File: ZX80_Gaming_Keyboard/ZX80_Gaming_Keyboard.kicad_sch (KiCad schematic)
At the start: 55 parts, among them J1 KB1, J2 KB2, J3 SPACE_ZERO, SW1 1, SW10 0, SW11 Q, SW12 W, SW13 E, SW14 R, SW15 T, SW16 Y, SW17 U, SW18 I, SW19 O, SW2 2, SW20 P, SW21 A, SW22 S, SW23 D, SW24 F, SW25 G, SW26 H, SW27 J, SW28 K, SW29 L, SW3 3, SW30 NL, SW31 SHIFT, SW32 Z, SW33 X, SW34 C, SW35 V, SW36 B, SW37 N, SW38 M, SW39 DOT, SW4 4, SW40 SPACE, SW41 LEFT, SW42 DOWN, SW43 UP, SW44 RIGHT, SW45 RUBOUT, SW5 5, SW6 6, SW7 7, SW8 8, SW9 9

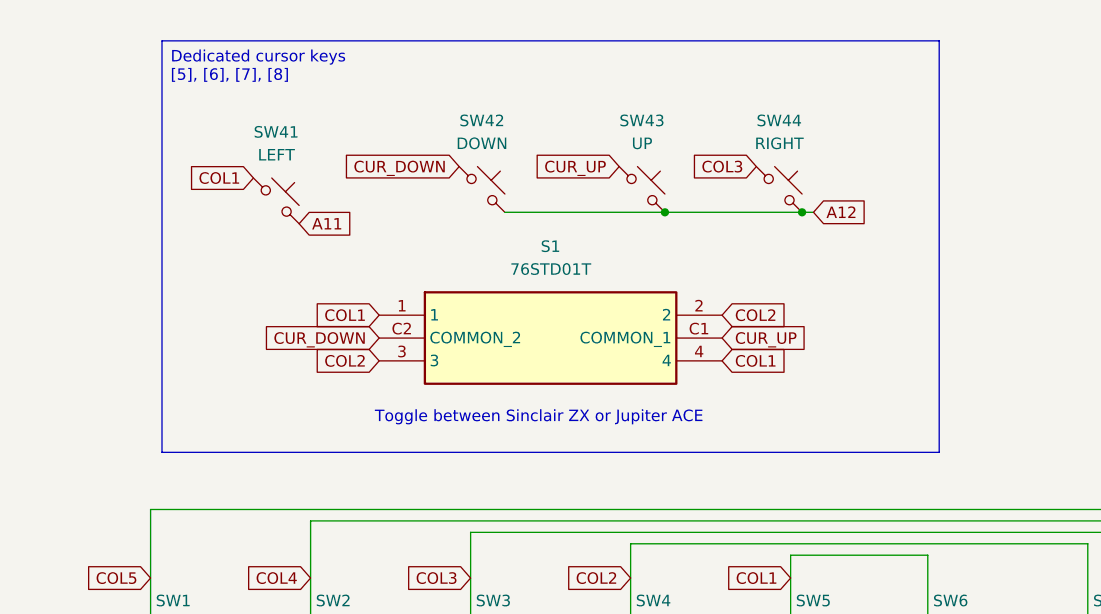
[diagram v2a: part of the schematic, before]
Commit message: Revised ZX/ACE switch
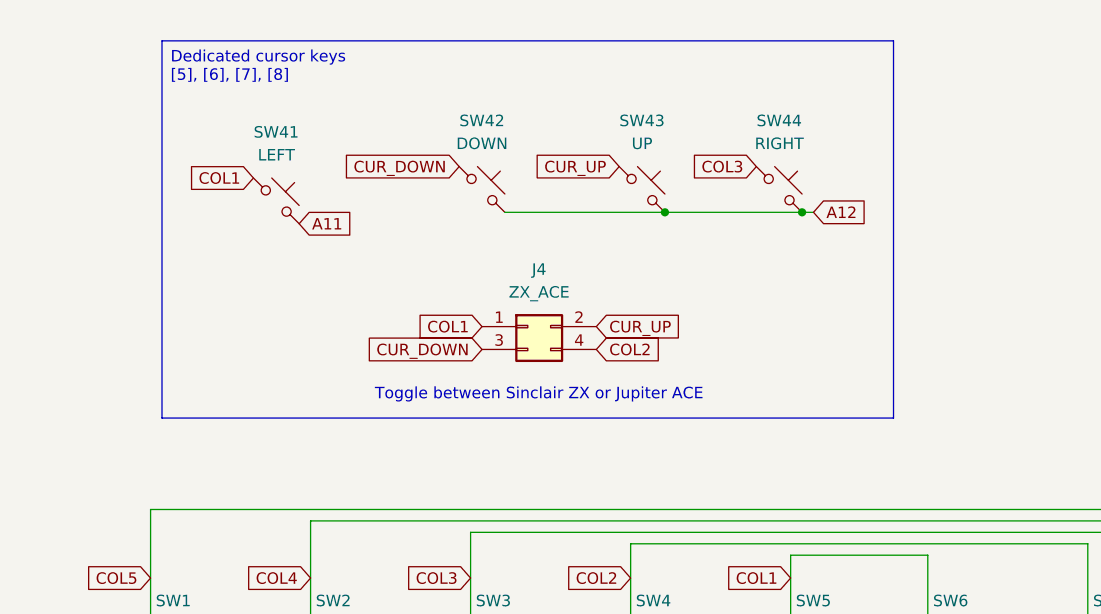
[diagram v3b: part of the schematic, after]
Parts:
- removed S1: 76STD01T, Button_Switch_THT:76STD01T, symbol Switch:76STD01T
- added J4: ZX_ACE, Connector_PinHeader_2.54mm:PinHeader_2x02_P2.54mm_Vertical, symbol Connector_Generic:Conn_02x02_Odd_Even
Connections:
- net COL1: now also J4.1 (Pin_1)
- net COL2: now also J4.4 (Pin_4)
- net CUR_DOWN: now also J4.3 (Pin_3)
- net CUR_UP: now also J4.2 (Pin_2)
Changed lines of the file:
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@@
 	(text "Toggle between Sinclair ZX or Jupiter ACE"
 		(exclude_from_sim no)
-		(at 124.46 62.23 0)
+		(at 124.46 59.69 0)
 		(effects
 			(font
@@
 		(exclude_from_sim no)
 		(at 82.55 20.32 0)
-		(size 86.36 45.72)
+		(size 81.28 41.91)
 		(margins 0.9525 0.9525 0.9525 0.9525)
 		(stroke
@@
 		)
 	)
-	(global_label "COL1"
+	(global_label "A10"
 		(shape input)
-		(at 106.68 50.8 180)
+		(at 123.19 165.1 180)
 		(fields_autoplaced yes)
 		(effects
@@
 		)
 		(property "Intersheetrefs" "${INTERSHEET_REFS}"
-			(at 98.8567 50.8 0)
+			(at 116.6972 165.1 0)
 			(effects
 				(font
@@
 		)
 	)
-	(global_label "A10"
+	(global_label "A11"
 		(shape input)
-		(at 123.19 165.1 180)
+		(at 97.79 40.64 0)
 		(fields_autoplaced yes)
 		(effects
@@
 				(size 1.27 1.27)
 			)
-			(justify right)
+			(justify left)
 		)
 		(property "Intersheetrefs" "${INTERSHEET_REFS}"
-			(at 116.6972 165.1 0)
+			(at 104.2828 40.64 0)
 			(effects
 				(font
 					(size 1.27 1.27)
 				)
-				(justify right)
+				(justify left)
 				(hide yes)
 			)
 		)
 	)
-	(global_label "A11"
+	(global_label "COL1"
 		(shape input)
-		(at 97.79 40.64 0)
+		(at 118.11 52.07 180)
 		(fields_autoplaced yes)
 		(effects
@@
 				(size 1.27 1.27)
 			)
-			(justify left)
+			(justify right)
 		)
 		(property "Intersheetrefs" "${INTERSHEET_REFS}"
-			(at 104.2828 40.64 0)
+			(at 110.2867 52.07 0)
 			(effects
 				(font
 					(size 1.27 1.27)
 				)
-				(justify left)
+				(justify right)
 				(hide yes)
 			)
@@
 		)
 	)
+	(global_label "CUR_DOWN"
+		(shape input)
+		(at 118.11 54.61 180)
+		(fields_autoplaced yes)
+		(effects
+			(font
+				(size 1.27 1.27)
+			)
+			(justify right)
+		)
+		(property "Intersheetrefs" "${INTERSHEET_REFS}"
+			(at 104.9043 54.61 0)
+			(effects
+				(font
+					(size 1.27 1.27)
+				)
+				(justify right)
+				(hide yes)
+			)
+		)
+	)
 	(global_label "A14"
 		(shape input)
@@
 		)
 	)
+	(global_label "COL2"
+		(shape input)
+		(at 130.81 54.61 0)
+		(fields_autoplaced yes)
+		(effects
+			(font
+				(size 1.27 1.27)
+			)
+			(justify left)
+		)
+		(property "Intersheetrefs" "${INTERSHEET_REFS}"
+			(at 138.6333 54.61 0)
+			(effects
+				(font
+					(size 1.27 1.27)
+				)
+				(justify left)
+				(hide yes)
+			)
+		)
+	)
 	(global_label "CUR_UP"
 		(shape input)
-		(at 144.78 53.34 0)
+		(at 130.81 52.07 0)
 		(fields_autoplaced yes)
 		(effects
@@
 		)
 		(property "Intersheetrefs" "${INTERSHEET_REFS}"
-			(at 155.2038 53.34 0)
+			(at 141.2338 52.07 0)
 			(effects
 				(font
@@
 		)
 	)
-	(global_label "COL2"
-		(shape input)
-		(at 144.78 50.8 0)
-		(fields_autoplaced yes)
-		(effects
-			(font
-				(size 1.27 1.27)
-			)
-			(justify left)
-		)
-		(property "Intersheetrefs" "${INTERSHEET_REFS}"
-			(at 152.6033 50.8 0)
-			(effects
-				(font
-					(size 1.27 1.27)
-				)
-				(justify left)
-				(hide yes)
-			)
-		)
-	)
 	(global_label "A9"
 		(shape input)
@@
 		)
 	)
-	(global_label "COL1"
-		(shape input)
-		(at 144.78 55.88 0)
-		(fields_autoplaced yes)
-		(effects
-			(font
-				(size 1.27 1.27)
-			)
-			(justify left)
-		)
-		(property "Intersheetrefs" "${INTERSHEET_REFS}"
-			(at 152.6033 55.88 0)
-			(effects
-				(font
-					(size 1.27 1.27)
-				)
-				(justify left)
-				(hide yes)
-			)
-		)
-	)
 	(global_label "A15"
 		(shape input)
@@
 	(global_label "CUR_DOWN"
 		(shape input)
-		(at 106.68 53.34 180)
-		(fields_autoplaced yes)
-		(effects
-			(font
-				(size 1.27 1.27)
-			)
-			(justify right)
-		)
-		(property "Intersheetrefs" "${INTERSHEET_REFS}"
-			(at 93.4743 53.34 0)
-			(effects
-				(font
-					(size 1.27 1.27)
-				)
-				(justify right)
-				(hide yes)
-			)
-		)
-	)
-	(global_label "CUR_DOWN"
-		(shape input)
 		(at 115.57 34.29 180)
 		(fields_autoplaced yes)
@@
 		)
 	)
-	(global_label "COL2"
-		(shape input)
-		(at 106.68 55.88 180)
-		(fields_autoplaced yes)
-		(effects
-			(font
-				(size 1.27 1.27)
-			)
-			(justify right)
-		)
-		(property "Intersheetrefs" "${INTERSHEET_REFS}"
-			(at 98.8567 55.88 0)
-			(effects
-				(font
-					(size 1.27 1.27)
-				)
-				(justify right)
-				(hide yes)
-			)
-		)
-	)
 	(global_label "COL1"
 		(shape input)
@@
 	)
 	(symbol
+		(lib_id "Connector_Generic:Conn_02x02_Odd_Even")
+		(at 123.19 52.07 0)
+		(unit 1)
+		(exclude_from_sim no)
+		(in_bom yes)
+		(on_board yes)
+		(dnp no)
+		(fields_autoplaced yes)
+		(property "Reference" "J4"
+			(at 124.46 45.72 0)
+			(effects
+				(font
+					(size 1.27 1.27)
+				)
+			)
+		)
+		(property "Value" "ZX_ACE"
+			(at 124.46 48.26 0)
+			(effects
+				(font
+					(size 1.27 1.27)
+				)
+			)
+		)
+		(property "Footprint" "Connector_PinHeader_2.54mm:PinHeader_2x02_P2.54mm_Vertical"
+			(at 123.19 52.07 0)
+			(effects
+				(font
+					(size 1.27 1.27)
+				)
+				(hide yes)
+			)
+		)
+		(property "Datasheet" "~"
+			(at 123.19 52.07 0)
+			(effects
+				(font
+					(size 1.27 1.27)
+				)
+				(hide yes)
+			)
+		)
+		(property "Description" "Generic connector, double row, 02x02, odd/even pin numbering scheme (row 1 odd numbers, row 2 even numbers), script generated (kicad-library-utils/schlib/autogen/connector/)"
+			(at 123.19 52.07 0)
+			(effects
+				(font
+					(size 1.27 1.27)
+				)
+				(hide yes)
+			)
+		)
+		(pin "1"
+		)
+		(pin "3"
+		)
+		(pin "4"
+		)
+		(pin "2"
+		)
+		(instances
+			(project ""
+				(path "/3757cb76-c3de-4d54-af41-21871afa6750"
+					(reference "J4")
+					(unit 1)
+				)
+			)
+		)
+	)
+	(symbol
 		(lib_id "Switch:SW_Push_45deg")
 		(at 241.3 90.17 0)
@@
 					(unit 1)
 				)
-			)
-		)
-	)
-	(symbol
-		(lib_id "Switch:76STD01T")
-		(at 106.68 50.8 0)
-		(unit 1)
-		(exclude_from_sim no)
-		(in_bom yes)
-		(on_board yes)
-		(dnp no)
-		(fields_autoplaced yes)
-		(property "Reference" "S1"
-			(at 125.73 43.18 0)
-			(effects
-				(font
-					(size 1.27 1.27)
-				)
-			)
-		)
-		(property "Value" "76STD01T"
-			(at 125.73 45.72 0)
-			(effects
-				(font
-					(size 1.27 1.27)
-				)
-			)
-		)
-		(property "Footprint" "Button_Switch_THT:76STD01T"
-			(at 140.97 145.72 0)
-			(effects
-				(font
-					(size 1.27 1.27)
-				)
-				(justify left top)
-				(hide yes)
-			)
-		)
-		(property "Datasheet" "https://datasheet.datasheetarchive.com/originals/distributors/Datasheets-DGA6/506009.pdf"
-			(at 140.97 245.72 0)
-			(effects
-				(font
-					(size 1.27 1.27)
-				)
-				(justify left top)
-				(hide yes)
-			)
-		)
-		(property "Description" "GRAYHILL - 76STD01T - SWITCH, DIP, 1 POSITION, DPDT, TOGGLE ROCKER"
-			(at 106.68 50.8 0)
-			(effects
-				(font
-					(size 1.27 1.27)
-				)
-				(hide yes)
-			)
-		)
-		(property "Height" "7.49"
-			(at 140.97 445.72 0)
-			(effects
-				(font
-					(size 1.27 1.27)
-				)
-				(justify left top)
-				(hide yes)
-			)
-		)
-		(property "Mouser Part Number" "706-76STD01T"
-			(at 140.97 545.72 0)
-			(effects
-				(font
-					(size 1.27 1.27)
-				)
-				(justify left top)
-				(hide yes)
-			)
-		)
-		(property "Mouser Price/Stock" "https://www.mouser.co.uk/ProductDetail/Grayhill/76STD01T?qs=ls7QRyWmRk4CM1%252BNOLs3Sg%3D%3D"
-			(at 140.97 645.72 0)
-			(effects
-				(font
-					(size 1.27 1.27)
-				)
-				(justify left top)
-				(hide yes)
-			)
-		)
-		(property "Manufacturer_Name" "Grayhill"
-			(at 140.97 745.72 0)
-			(effects
-				(font
-					(size 1.27 1.27)
-				)
-				(justify left top)
-				(hide yes)
-			)
-		)
-		(property "Manufacturer_Part_Number" "76STD01T"
-			(at 140.97 845.72 0)
-			(effects
-				(font
-					(size 1.27 1.27)
-				)
-				(justify left top)
-				(hide yes)
-			)
-		)
-		(pin "1"
-		)
-		(pin "3"
-		)
-		(pin "2"
-		)
-		(pin "C1"
-		)
-		(pin "4"
-		)
-		(pin "C2"
-		)
-		(instances
-			(project ""
-				(path "/3757cb76-c3de-4d54-af41-21871afa6750"
-					(reference "S1")
-					(unit 1)
-				)

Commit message: Initial Rev. C changes
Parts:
- removed D1: 1N4148, Diode_THT:D_DO-35_SOD27_P7.62mm_Horizontal, symbol Device:D
- renumbered D2 to D1
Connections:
- net A8: now also D1.2 (A), SW45.2
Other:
- moved on the sheet: D1
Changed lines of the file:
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@@
 	(title_block
 		(title "ZX80 Gaming Keyboard")
-		(date "15-Jun-2025")
-		(rev "B")
+		(date "27-Jun-2025")
+		(rev "C")
 		(company "Brett Hallen")
 		(comment 1 "www.youtube.com/@Brfff")
@@
 	(wire
 		(pts
-			(xy 229.87 40.64) (xy 226.06 40.64)
-		)
-		(stroke
-			(width 0)
-			(type default)
-		)
-	)
-	(wire
-		(pts
 			(xy 116.84 87.63) (xy 116.84 106.68)
 		)
@@
 	(global_label "A8"
 		(shape input)
-		(at 237.49 35.56 0)
+		(at 229.87 35.56 0)
 		(fields_autoplaced yes)
 		(effects
@@
 		)
 		(property "Intersheetrefs" "${INTERSHEET_REFS}"
-			(at 242.7733 35.56 0)
+			(at 235.1533 35.56 0)
 			(effects
 				(font
@@
 	(global_label "A12"
 		(shape input)
-		(at 237.49 40.64 0)
+		(at 233.68 40.64 0)
 		(fields_autoplaced yes)
 		(effects
@@
 		)
 		(property "Intersheetrefs" "${INTERSHEET_REFS}"
-			(at 243.9828 40.64 0)
+			(at 240.1728 40.64 0)
 			(effects
 				(font
@@
 	(symbol
 		(lib_id "Device:D")
-		(at 233.68 40.64 180)
+		(at 229.87 40.64 180)
 		(unit 1)
 		(exclude_from_sim no)
@@
 		(on_board yes)
 		(dnp no)
-		(property "Reference" "D2"
-			(at 232.41 43.18 0)
+		(property "Reference" "D1"
+			(at 228.6 43.18 0)
 			(effects
 				(font
@@
 		)
 		(property "Value" "1N4148"
-			(at 231.14 45.72 0)
+			(at 227.33 45.72 0)
 			(effects
 				(font
@@
 		)
 		(property "Footprint" "Diode_THT:D_DO-35_SOD27_P7.62mm_Horizontal"
-			(at 233.68 40.64 0)
+			(at 229.87 40.64 0)
 			(effects
 				(font
@@
 		)
 		(property "Datasheet" "~"
-			(at 233.68 40.64 0)
+			(at 229.87 40.64 0)
 			(effects
 				(font
@@
 		)
 		(property "Description" "Diode"
-			(at 233.68 40.64 0)
+			(at 229.87 40.64 0)
 			(effects
 				(font
@@
 		)
 		(property "Sim.Device" "D"
-			(at 233.68 40.64 0)
+			(at 229.87 40.64 0)
 			(effects
 				(font
@@
 		)
 		(property "Sim.Pins" "1=K 2=A"
-			(at 233.68 40.64 0)
+			(at 229.87 40.64 0)
 			(effects
 				(font
@@
 			(project ""
 				(path "/3757cb76-c3de-4d54-af41-21871afa6750"
-					(reference "D2")
+					(reference "D1")
 					(unit 1)
 				)
@@
 					(unit 1)
 				)
-			)
-		)
-	)
-	(symbol
-		(lib_id "Device:D")
-		(at 233.68 35.56 180)
-		(unit 1)
-		(exclude_from_sim no)
-		(in_bom yes)
-		(on_board yes)
-		(dnp no)
-		(fields_autoplaced yes)
-		(property "Reference" "D1"
-			(at 233.68 29.21 0)
-			(effects
-				(font
-					(size 1.27 1.27)
-				)
-			)
-		)
-		(property "Value" "1N4148"
-			(at 233.68 31.75 0)
-			(effects
-				(font
-					(size 1.27 1.27)
-				)
-			)
-		)
-		(property "Footprint" "Diode_THT:D_DO-35_SOD27_P7.62mm_Horizontal"
-			(at 233.68 35.56 0)
-			(effects
-				(font
-					(size 1.27 1.27)
-				)
-				(hide yes)
-			)
-		)
-		(property "Datasheet" "~"
-			(at 233.68 35.56 0)
-			(effects
-				(font
-					(size 1.27 1.27)
-				)
-				(hide yes)
-			)
-		)
-		(property "Description" "Diode"
-			(at 233.68 35.56 0)
-			(effects
-				(font
-					(size 1.27 1.27)
-				)
-				(hide yes)
-			)
-		)
-		(property "Sim.Device" "D"
-			(at 233.68 35.56 0)
-			(effects
-				(font
-					(size 1.27 1.27)
-				)
-				(hide yes)
-			)
-		)
-		(property "Sim.Pins" "1=K 2=A"
-			(at 233.68 35.56 0)
-			(effects
-				(font
-					(size 1.27 1.27)
-				)
-				(hide yes)
-			)
-		)
-		(pin "1"
-		)
-		(pin "2"
-		)
-		(instances
-			(project ""
-				(path "/3757cb76-c3de-4d54-af41-21871afa6750"
-					(reference "D1")
-					(unit 1)
-				)
